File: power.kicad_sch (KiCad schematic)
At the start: 58 parts, among them U10 MAX4495AAUT, U11 MAX4495ALAUT, U4 TPSM828302ARDSR, U5 LP3962EMP-3.3/NOPB, U6 STWD100NYWY3F, U7 STWD100NYWY3F, U8 MP5073GG-P, U9 MAX4495AAUT

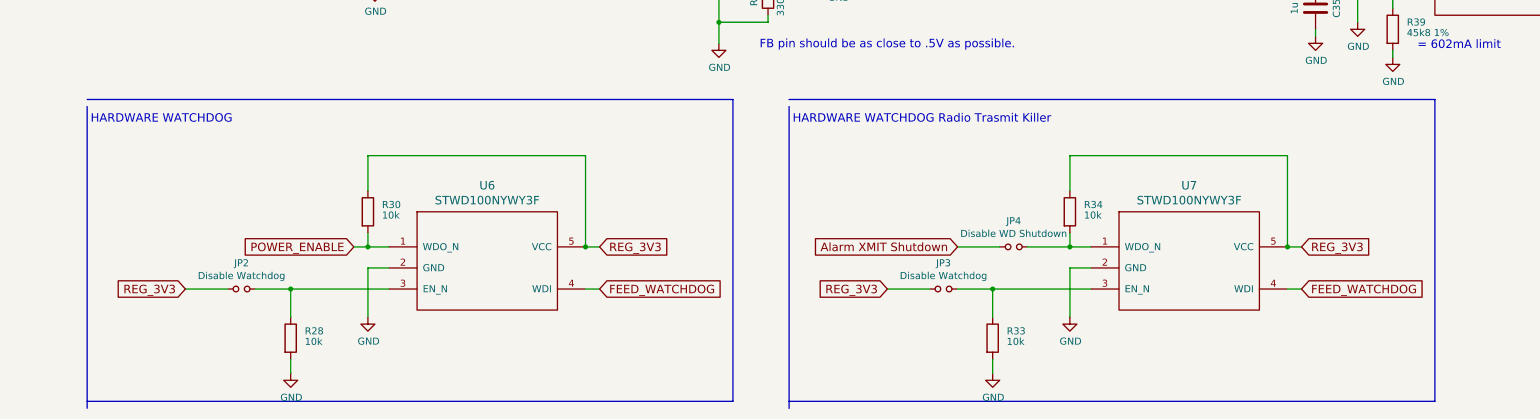
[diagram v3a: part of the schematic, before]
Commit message: Remove the PA watchdog
It wasn't doing anything useful.

Add an enable line from the processor to the TX AX5043.

Signed-off-by: Corey Minyard <corey@minyard.net>
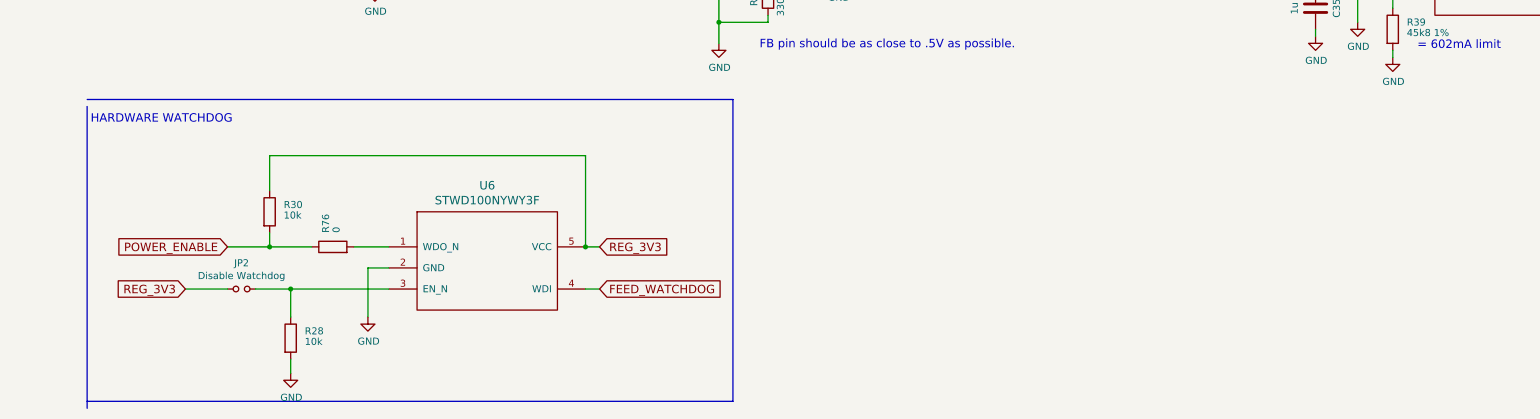
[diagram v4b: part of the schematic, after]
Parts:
- removed JP3: Disable Watchdog, Jumper:SolderJumper-2_P1.3mm_Open_RoundedPad1.0x1.5mm, symbol PACSAT_DEV_misc:Jumper_NO_Small
- removed JP4: Disable WD Shutdown, Jumper:SolderJumper-2_P1.3mm_Open_RoundedPad1.0x1.5mm, symbol PACSAT_DEV_misc:Jumper_NO_Small
- removed R33, R34: 10k, Resistor_SMD:R_0603_1608Metric_Pad0.98x0.95mm_HandSolder, symbol Device:R
- removed U7: STWD100NYWY3F, Package_TO_SOT_SMD:SOT-23-5_HandSoldering, symbol PACSAT_ICs:STWD100NYWY3F
- added R76: 0, Resistor_SMD:R_0603_1608Metric_Pad0.98x0.95mm_HandSolder, symbol Device:R
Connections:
- net POWER_ENABLE: now also R76.1; no longer U6.1 (WDO_N)
- new net: R76.2, U6.1 (WDO_N)
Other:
- note removed: "HARDWARE WATCHDOG Radio Trasmit Killer"
- moved on the sheet: R30

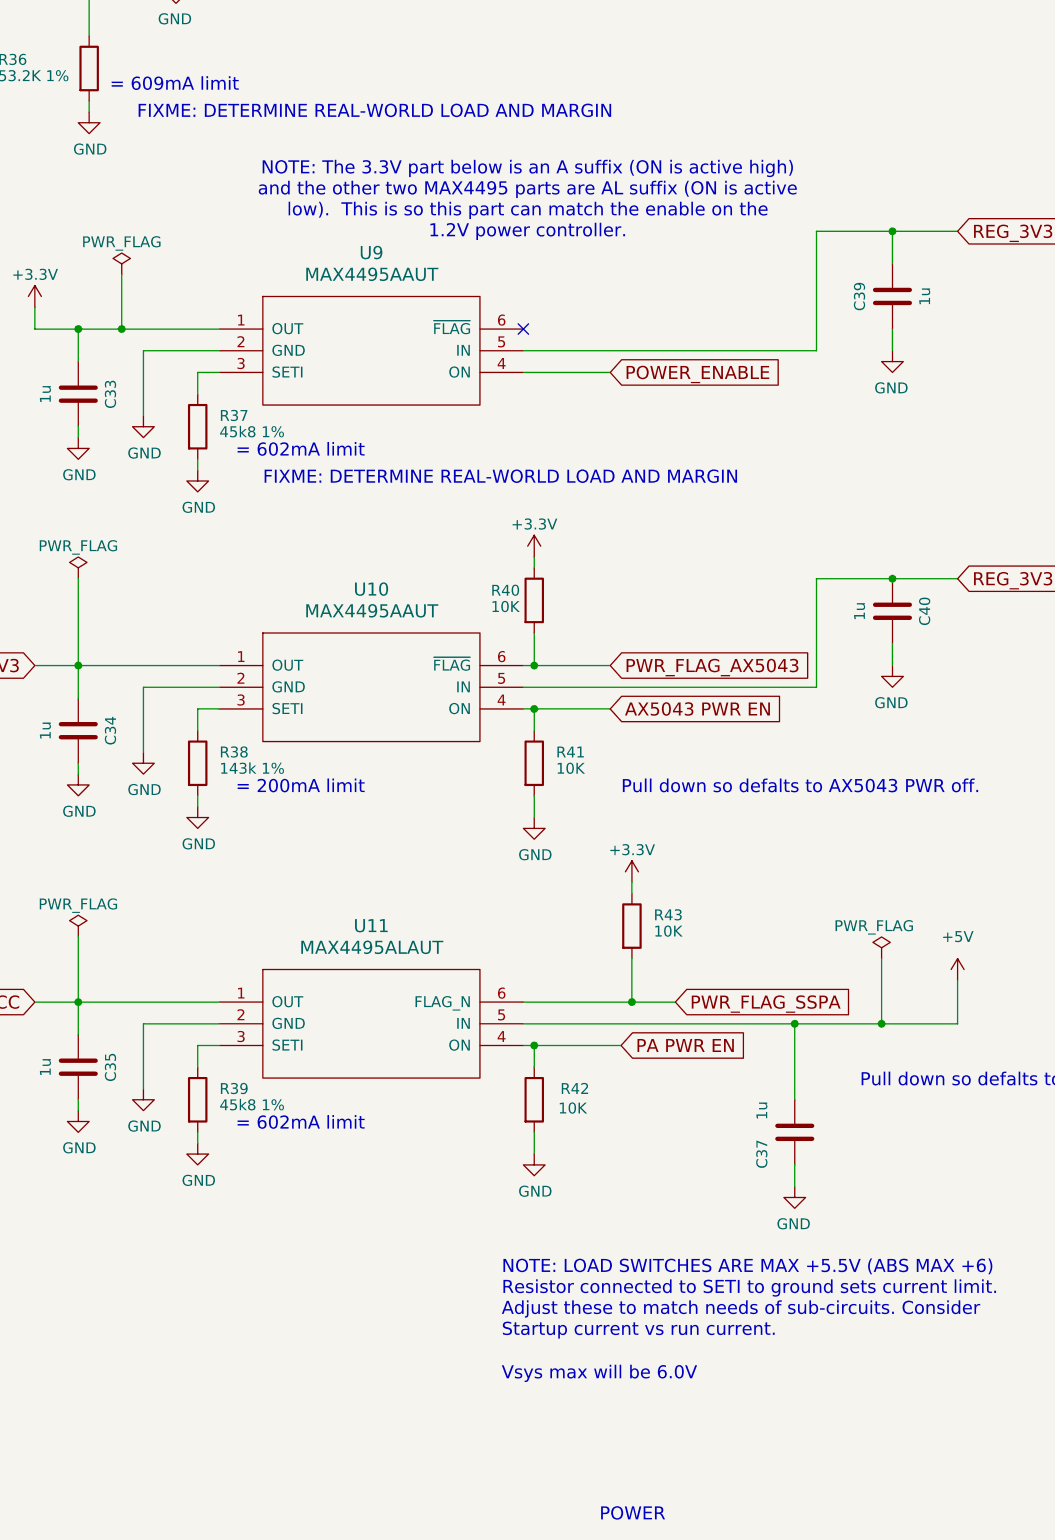
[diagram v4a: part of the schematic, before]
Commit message: Work on the power section
Move things over to the left a little bit to give more room on the
right side of the board.

Signed-off-by: Corey Minyard <corey@minyard.net>
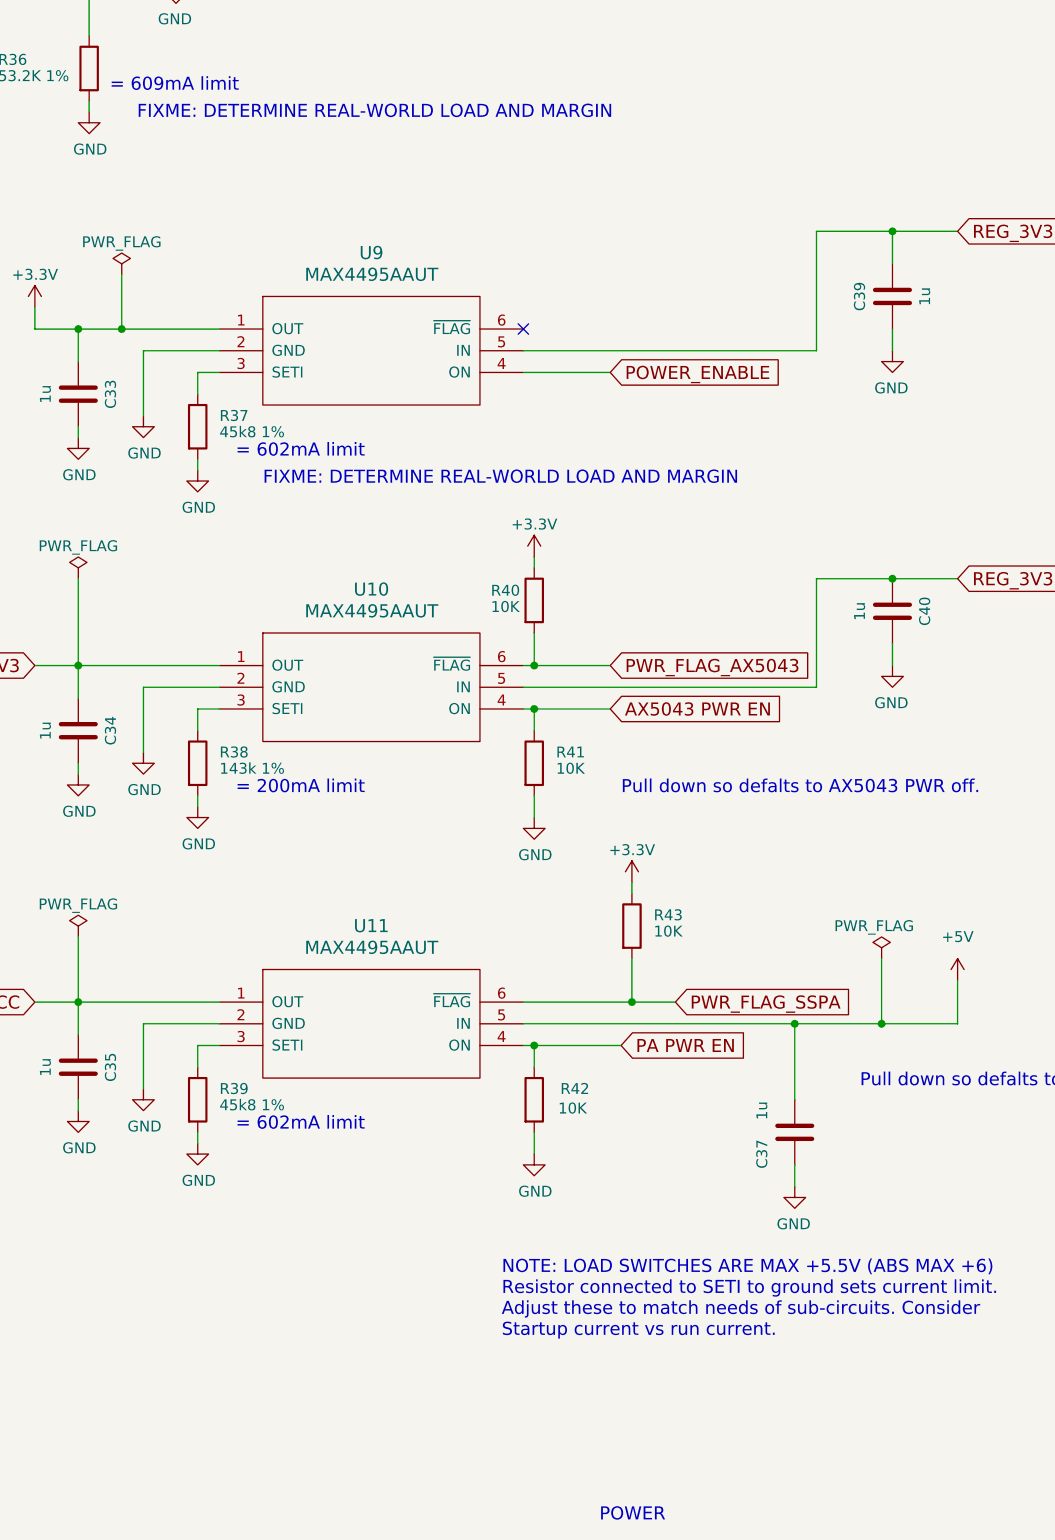
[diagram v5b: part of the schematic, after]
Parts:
- U11: value MAX4495ALAUT -> MAX4495AAUT; symbol PACSAT_ICs:MAX4995ALAUT -> PACSAT_ICs:MAX4995AAUT
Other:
- note removed: "NOTE: The 3.3V part below is an A suffix (ON is active high) and the other two MAX4495 parts are AL suffix (ON is active low). This is so this part can match the enable on the 1.2V power controller."
- note removed: "Vsys max will be 6.0V"
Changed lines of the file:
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@@
 		)
 	)
-	(text "Vsys max will be 6.0V"
-		(exclude_from_sim no)
-		(at 322.58 228.6 0)
-		(effects
-			(font
-				(size 1.524 1.524)
-			)
-			(justify left bottom)
-		)
-	)
 	(text ".1ms soft-start time"
 		(exclude_from_sim no)
@@
 		)
 	)
-	(text "NOTE: The 3.3V part below is an A suffix (ON is active high)\nand the other two MAX4495 parts are AL suffix (ON is active\nlow).  This is so this part can match the enable on the\n1.2V power controller."
-		(exclude_from_sim no)
-		(at 325.628 90.424 0)
-		(effects
-			(font
-				(size 1.524 1.524)
-			)
-		)
-	)
 	(text "Enable at Powerup"
 		(exclude_from_sim no)
@@
 	)
 	(symbol
-		(lib_id "PACSAT_ICs:MAX4995ALAUT")
+		(lib_id "PACSAT_ICs:MAX4995AAUT")
 		(at 307.34 186.69 0)
 		(unit 1)
@@
 			)
 		)
-		(property "Value" "MAX4495ALAUT"
+		(property "Value" "MAX4495AAUT"
 			(at 307.34 177.8 0)
 			(effects

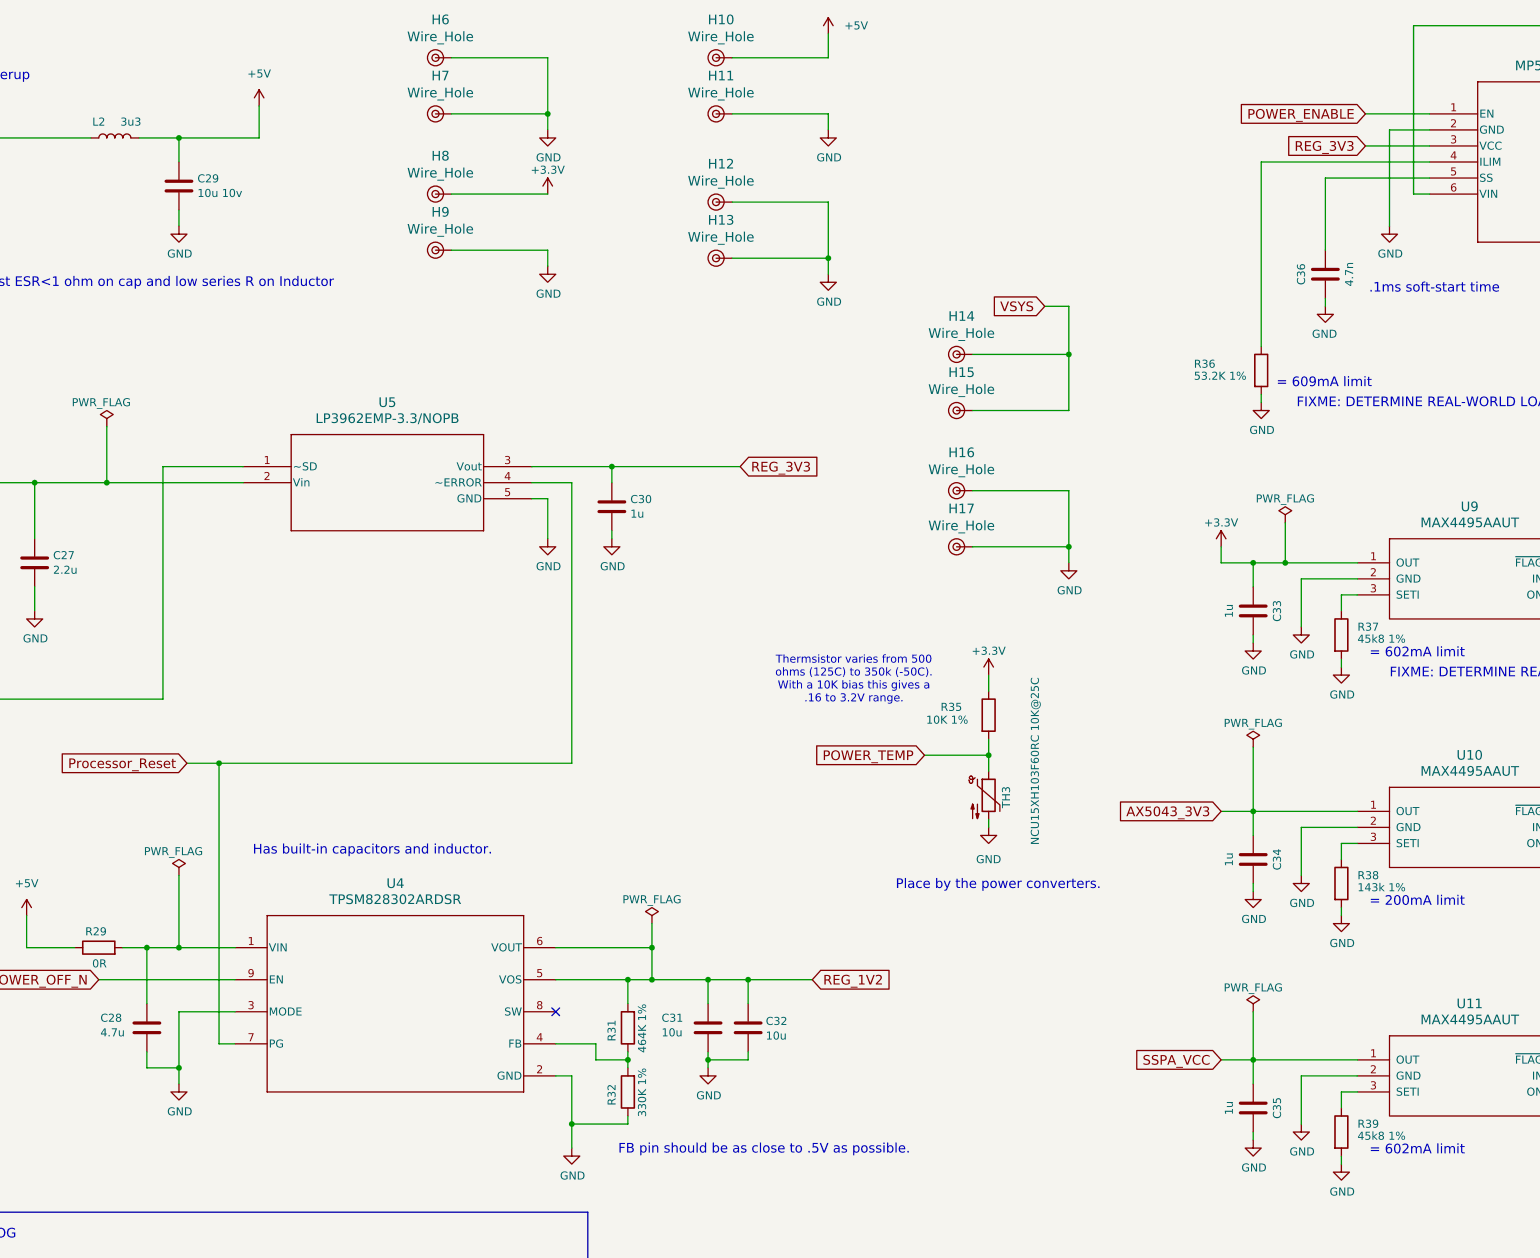
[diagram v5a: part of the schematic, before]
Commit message: Fix values of a lot of parts
Make them standard, 4.1p instead of 4p1, etc.

Add a tag to a couple of ICs that didn't have a pin 1 indicator on the
board.

Signed-off-by: Corey Minyard <corey@minyard.net>
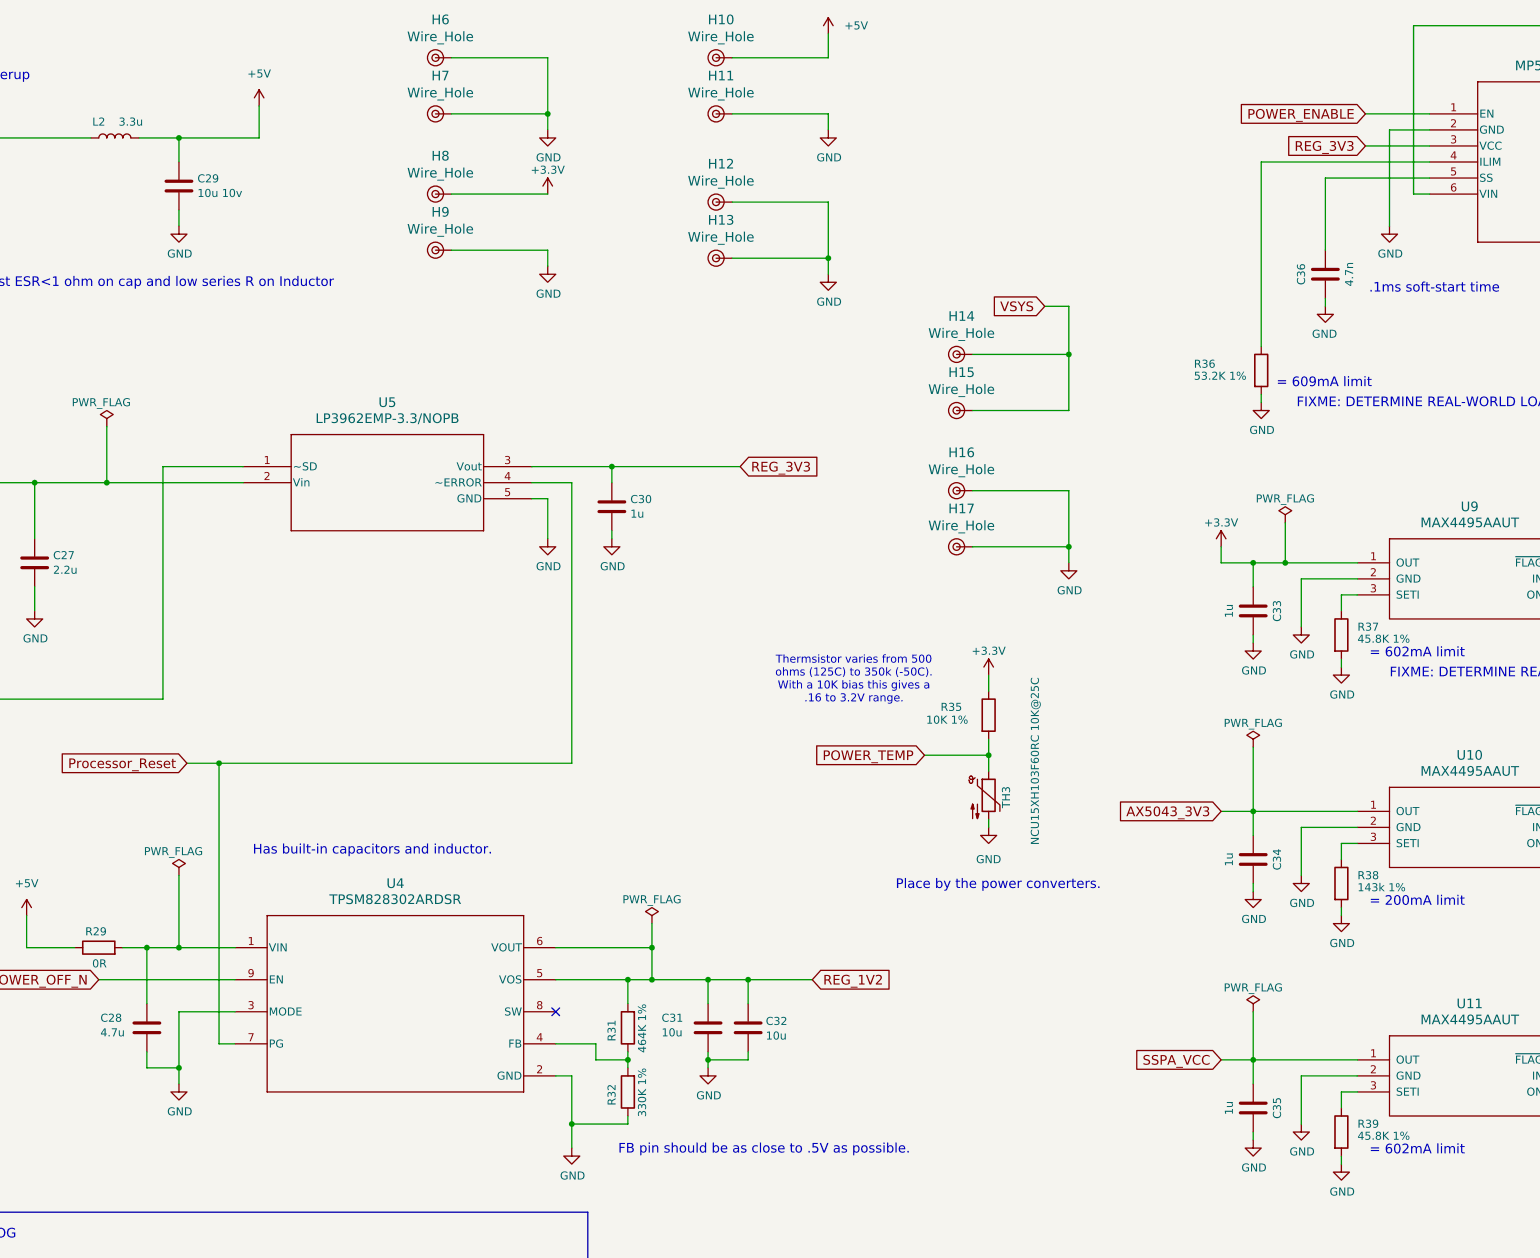
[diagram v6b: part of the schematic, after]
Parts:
- L2: value 3u3 -> 3.3u
- R37, R39: value 45k8 1% -> 45.8K 1%
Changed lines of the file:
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@@
 			)
 		)
-		(property "Value" "45k8 1%"
+		(property "Value" "45.8K 1%"
 			(at 289.56 196.215 0)
 			(effects
@@
 			)
 		)
-		(property "Value" "45k8 1%"
+		(property "Value" "45.8K 1%"
 			(at 289.56 117.475 0)
 			(effects
@@
 			)
 		)
-		(property "Value" "3u3"
+		(property "Value" "3.3u"
 			(at 95.25 35.56 90)
 			(effects
